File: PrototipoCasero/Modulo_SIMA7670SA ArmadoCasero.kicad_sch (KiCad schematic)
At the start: 41 parts, among them J1 TBP01R1-508-02BE, J2 Jack DC 2.1mm PCB recto, J3 DB9 Hembra Impreso 90°, Q1 BC327, Q2 2N7000, U1 24LC512, U2 LM7805_TO220, U3 LM2596S_Modulo_Regulable, U4 Black_Pill_STM32F411CEUx, U5 MAX232, U6 BKP-A7670SA (Módulo SIMCOM)

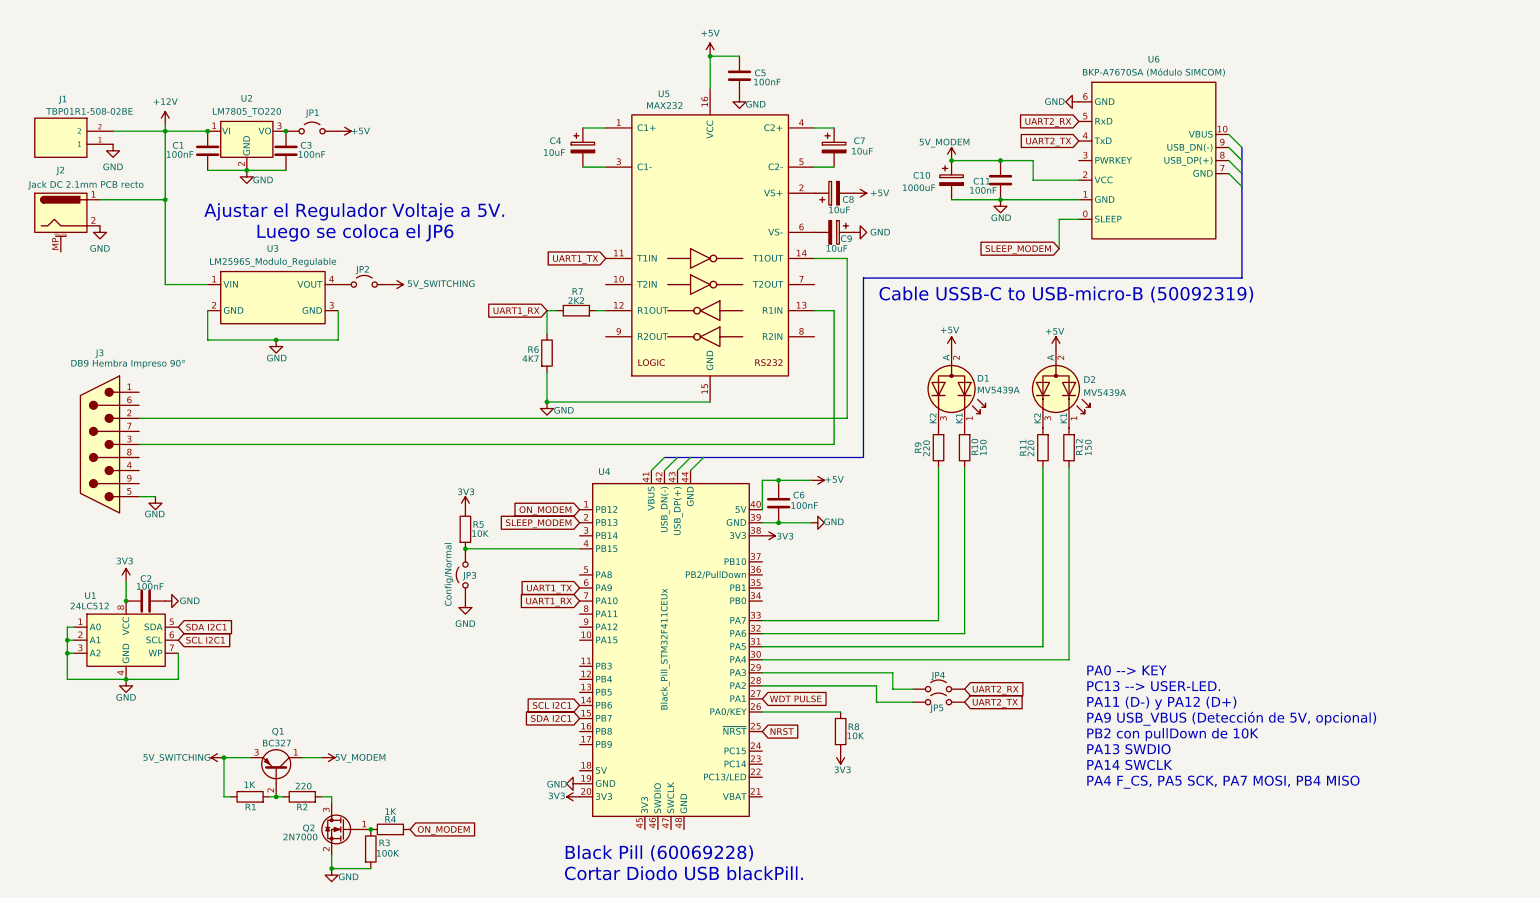
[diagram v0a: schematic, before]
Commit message: Se hicieron modificaciones en los circuitos mosfet para controlar on/off del BKP-A7670SA y de la 24C512.
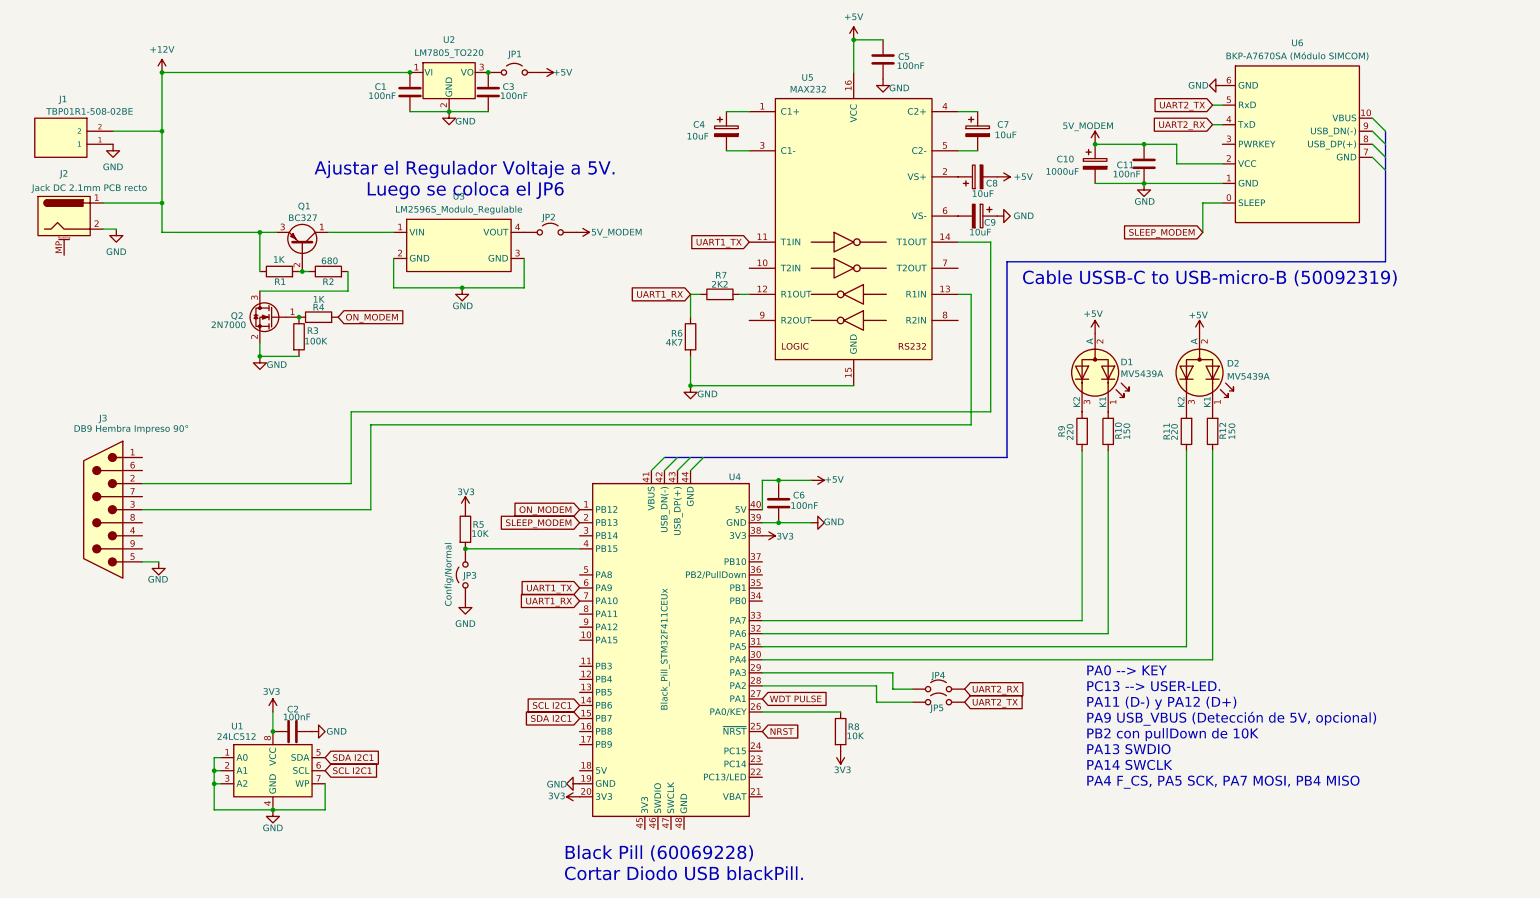
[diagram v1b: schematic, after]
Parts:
- R2: value 220 -> 680
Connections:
- net +12V: now also Q1.3 (E), R1.1; no longer U3.1 (VIN)
- net 5V_MODEM: now also JP2.2 (B); no longer Q1.1 (C)
- net UART2_RX: now also U6.4 (TxD); no longer U6.5 (RxD)
- net UART2_TX: now also U6.5 (RxD); no longer U6.4 (TxD)
- removed net 5V_SWITCHING: JP2.2 (B), Q1.3 (E), R1.1
- new net: Q1.1 (C), U3.1 (VIN)
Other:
- moved on the sheet: C1, C10, C11, C2, C3, C4, C5, C7, C8, C9, D1, D2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
